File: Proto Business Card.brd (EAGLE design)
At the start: 88.9 x 50.8 mm, 551 parts

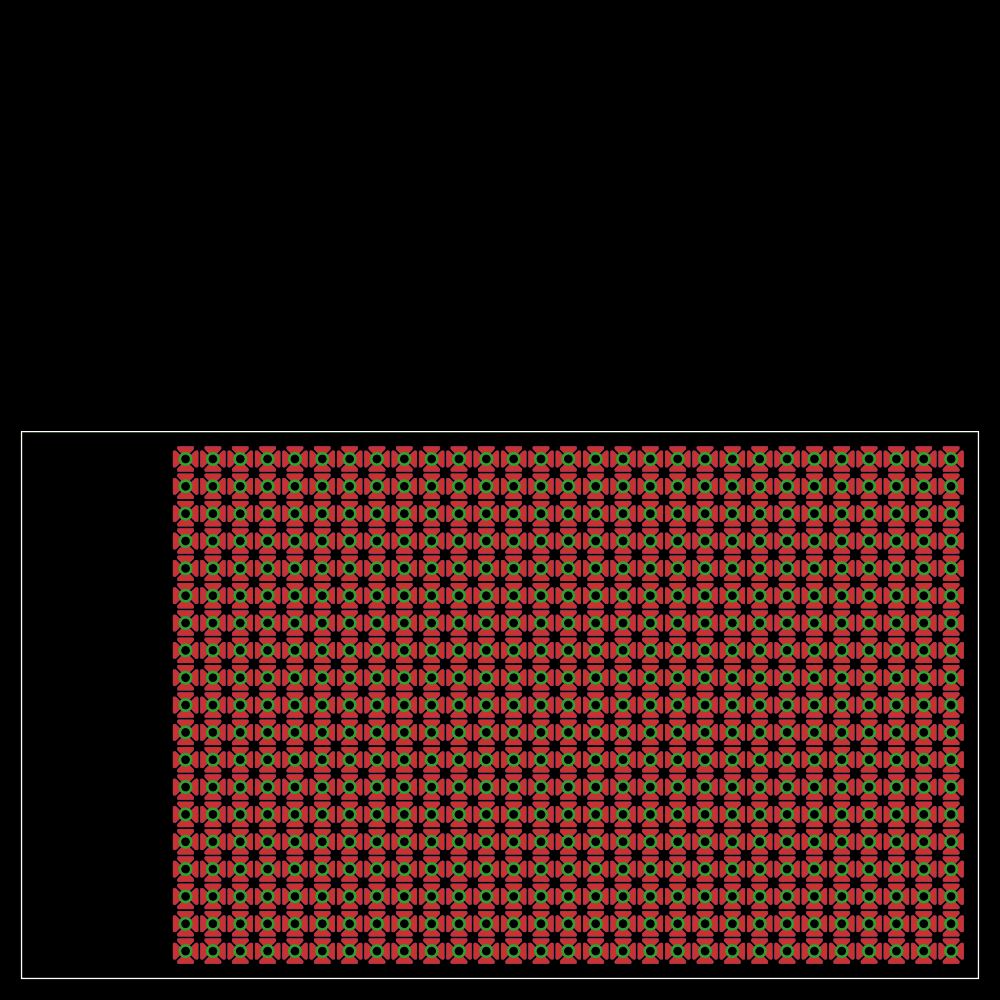
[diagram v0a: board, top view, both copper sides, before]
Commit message: Text is now on, and the grid is complete. Still missing example layers on the back
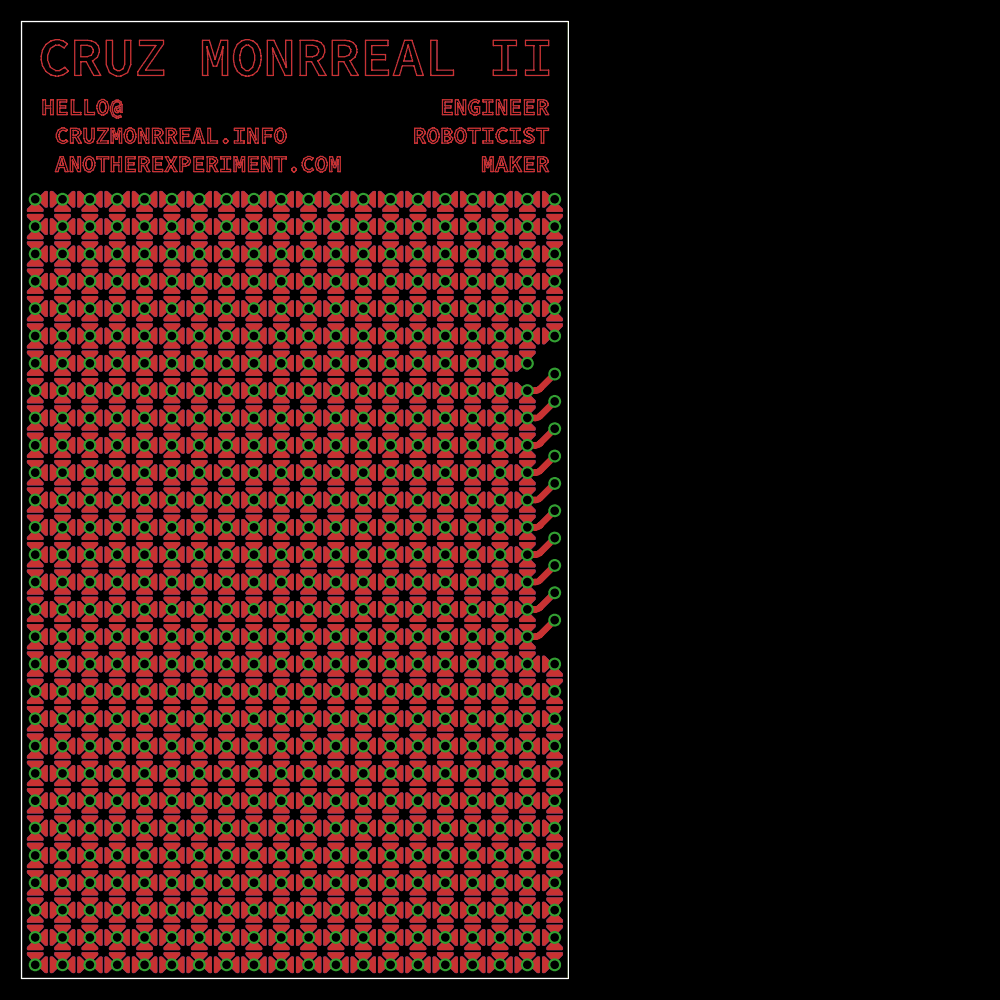
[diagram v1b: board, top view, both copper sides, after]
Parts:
- removed U$576, U$577, U$578, U$579, U$580, U$581, U$582, U$583, U$584, U$589, U$596, U$597, U$598, U$599, U$600, U$601, U$602, U$603, U$604, U$605, U$606, U$607, U$608, U$609, U$610, U$611, U$612, U$613, U$614, U$621, U$622, U$623, U$624, U$625, U$626, U$627, U$628, U$629, U$630, U$631, U$632, U$633, U$634, U$635, U$636, U$637, U$638, U$639: VIA.4-4, flowerpad:4-4
- added U$100, U$148, U$149, U$74, U$75, U$95, U$96, U$97, U$98, U$99: VIA.NONE, flowerpad:NONE
- added U$120, U$121, U$122, U$123, U$124, U$125, U$145, U$146, U$150, U$20, U$22, U$23, U$24, U$25, U$45, U$46, U$501, U$502, U$566, U$567, U$568, U$569: VIA.3-3, flowerpad:3-3
- added U$147, U$171, U$172, U$173, U$174, U$175, U$47, U$48, U$49, U$497, U$498, U$499, U$50, U$500, U$503, U$504, U$505, U$506, U$507, U$508, U$509, U$510, U$511, U$512, U$515, U$516, U$517, U$518, U$519, U$520, U$540, U$541, U$542, U$543, U$544, U$545, U$565, U$70, U$71, U$72, U$73: VIA.4-4, flowerpad:4-4
- added U$170, U$21, U$570: VIA.2-2.CORNER, flowerpad:2-2.CORNER
- U$1, U$3, U$37, U$574, U$575: value VIA.4-4 -> VIA.2-2.CORNER; device flowerpad:4-4 -> flowerpad:2-2.CORNER
- U$10, U$11, U$112, U$113, U$12, U$13, U$14, U$15, U$152, U$153, U$16, U$17, U$18, U$182, U$183, U$19, U$2, U$211, U$212, U$240, U$241, U$26, U$269, U$27, U$270, U$28, U$29, U$298, U$299, U$30, U$31, U$32, U$327, U$328, U$33, U$34, U$35, U$356, U$357, U$36, U$385, U$386, U$4, U$414, U$415, U$443, U$444, U$472, U$473, U$5, U$530, U$531, U$559, U$560, U$571, U$572, U$573, U$588, U$6, U$7, U$77, U$78, U$8, U$9: value VIA.4-4 -> VIA.3-3; device flowerpad:4-4 -> flowerpad:3-3
- moved U$208 82.4 mm to (14.0, 8.89)
- moved U$240 81.5 mm to (16.5, 1.27), turned to 270 degrees
- moved U$207 79.0 mm to (14.0, 11.4)
- moved U$239 78.0 mm to (16.5, 3.81)
- moved U$1 77.8 mm to (49.5, 72.4)
- moved U$415 75.6 mm to (34.3, 72.4), turned to 90 degrees
- moved U$206 75.5 mm to (14.0, 14.0)
- moved U$416 75.5 mm to (34.3, 69.8)
- moved U$238 74.5 mm to (16.5, 6.35)
- moved U$444 73.6 mm to (36.8, 72.4), turned to 90 degrees
- moved U$473 73.4 mm to (39.4, 72.4), turned to 90 degrees
- moved U$445 72.9 mm to (36.8, 69.8)
- moved U$446 72.4 mm to (36.8, 67.3)
- moved U$205 72.1 mm to (14.0, 16.5)
- moved U$474 72.1 mm to (39.4, 69.8)
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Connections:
- new net N$1: U$145.VIA, U$99.VIA
- new net N$10: U$149.VIA, U$170.VIA
- new net N$2: U$100.VIA, U$146.VIA
- new net N$3: U$124.VIA, U$97.VIA
- new net N$4: U$125.VIA, U$98.VIA
- new net N$5: U$122.VIA, U$95.VIA
- new net N$6: U$123.VIA, U$96.VIA
- new net N$7: U$120.VIA, U$74.VIA
- new net N$8: U$121.VIA, U$75.VIA
- new net N$9: U$148.VIA, U$150.VIA
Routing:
- net N$16: track 0.00 -> 21.9 mm
- net N$19: track 0.00 -> 19.5 mm
- net N$24: track 0.00 -> 16.4 mm
- net N$15: track 0.00 -> 15.4 mm
- net N$14: track 0.00 -> 15.4 mm
- net N$29: track 0.00 -> 14.0 mm
- net N$28: track 0.00 -> 14.0 mm
- net N$12: track 0.00 -> 13.3 mm
- net N$20: track 0.00 -> 13.3 mm
- net N$22: track 0.00 -> 13.3 mm
- net N$11: track 0.00 -> 13.0 mm
- net N$26: track 0.00 -> 11.7 mm
- net N$27: track 0.00 -> 10.7 mm
- net N$17: track 0.00 -> 9.52 mm
- net N$87: track 0.00 -> 9.30 mm
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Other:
- board size 88.9 x 50.8 mm -> 50.8 x 88.9 mm
- board text removed: "CRUZ MONRREAL II"
- board text removed: "CRUZ.MONRREAL@GMAIL.COM"
- board text removed: "ENGINEER | FABRICATOR | PROGRAMMER"
